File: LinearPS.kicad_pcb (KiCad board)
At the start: 2 copper layers, 100 x 100 mm, 100 parts, among them J1 Conn_01x03, J10 Conn_01x01, J11 Conn_01x01, J12 Conn_01x01, J14 Conn_01x01, J2 Conn_01x02, J3 Conn_01x03, J4 Conn_01x01, J5 Conn_01x01, J6 Conn_01x01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

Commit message: Fixed several layout issues, added a couple of resistors to ensure stability
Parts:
- added R33: 1k, Resistors_THT:R_Axial_DIN0411_L9.9mm_D3.6mm_P12.70mm_Horizontal, F.Cu at (147.5, 141.0)
- added R35: 1M, Resistors_THT:R_Axial_DIN0207_L6.3mm_D2.5mm_P7.62mm_Horizontal, F.Cu at (118.5, 62.0)
- R24, R25, R26, R27, R7: value 0R24 -> 0R47
- moved J2 10.4 mm to (141.9, 118.0)
- moved R17 9.19 mm to (140.8, 67.4)
- moved R40 6.93 mm to (120.7, 64.8), turned to 0 degrees
- moved J9 3.56 mm to (142.4, 60.5)
- moved U3 2.86 mm to (127.6, 75.4)
- moved R29 0.90 mm to (129.8, 81.8)
- moved RV2 0.49 mm to (142.5, 71.8)
- moved C14 0.28 mm to (136.7, 64.8)
- moved R38 0.21 mm to (128.3, 62.0)
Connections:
- Q2 pad 1: Net-(C9-Pad1) -> Net-(Q2-Pad1)
- R29 pad 1: Net-(R29-Pad1) -> GND
- R29 pad 2: GND -> Net-(R29-Pad2)
- R34 pad 1: Net-(JP4-Pad3) -> Net-(JP4-Pad1)
- R34 pad 2: Net-(R29-Pad1) -> Net-(R29-Pad2)
- RV2 pad 2: Net-(JP4-Pad1) -> Net-(JP4-Pad3)
- U3 pad 1: Net-(JP4-Pad3) -> Net-(JP4-Pad1)
- U3 pad 2: Net-(R29-Pad1) -> Net-(R29-Pad2)
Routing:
- net Net-(J9-Pad2): track 22.0 -> 50.0 mm
- net Net-(C9-Pad1): track 105.2 -> 78.3 mm
- net Net-(JP4-Pad1): track 53.3 -> 31.4 mm
- net Net-(JP4-Pad3): track 39.5 -> 60.8 mm
- net Net-(Q2-Pad1): track 0.00 -> 15.0 mm
- net Net-(R29-Pad2): track 0.00 -> 12.5 mm
- net Net-(C4-Pad1): track 172.2 -> 160.2 mm
- net Net-(R29-Pad1): track 12.0 -> 0.00 mm
- net Net-(C15-Pad1): track 19.9 -> 9.43 mm
- net Net-(R17-Pad1): track 15.2 -> 5.61 mm
- net Net-(C6-Pad1): track 162.0 -> 152.5 mm
- net Net-(JP5-Pad3): track 29.3 -> 23.6 mm
- net Net-(Q2-Pad3): track 172.2 -> 166.9 mm
- net Net-(J9-Pad1): track 34.7 -> 39.1 mm
- net Net-(C15-Pad2): track 26.7 -> 23.8 mm
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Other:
- board text added: "CONSTANT CURRENT, CONSTANT VOLTAGE SUPPLY 0-30 VDC, 20 mA-10 A PCB D MARKS CC-BY-SA 4.0"
- board text removed: "CONSTANT CURRENT, CONSTANT VOLTAGE SUPPLY 0-30 VDC, 20 mA-20 A PCB D MARKS CC-BY-SA 4.0"

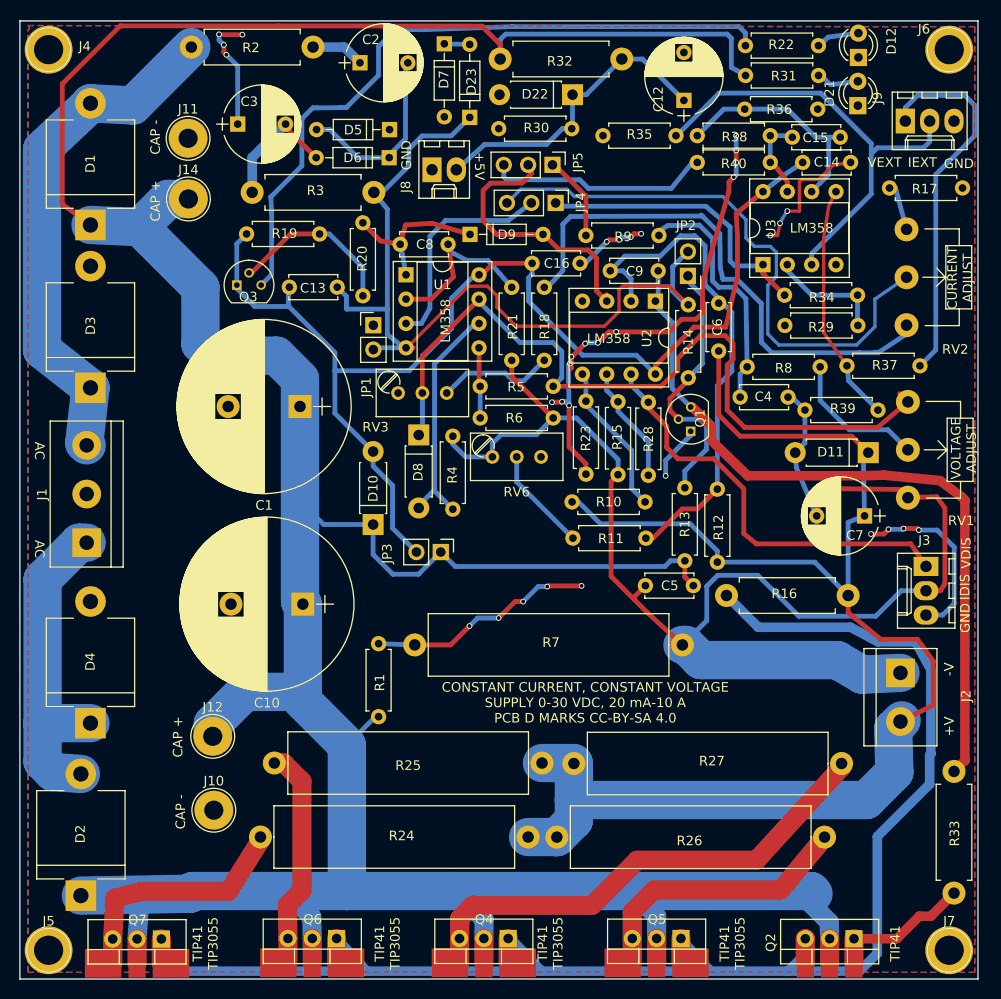
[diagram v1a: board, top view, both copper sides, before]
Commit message: Added extra pin to get reference voltage
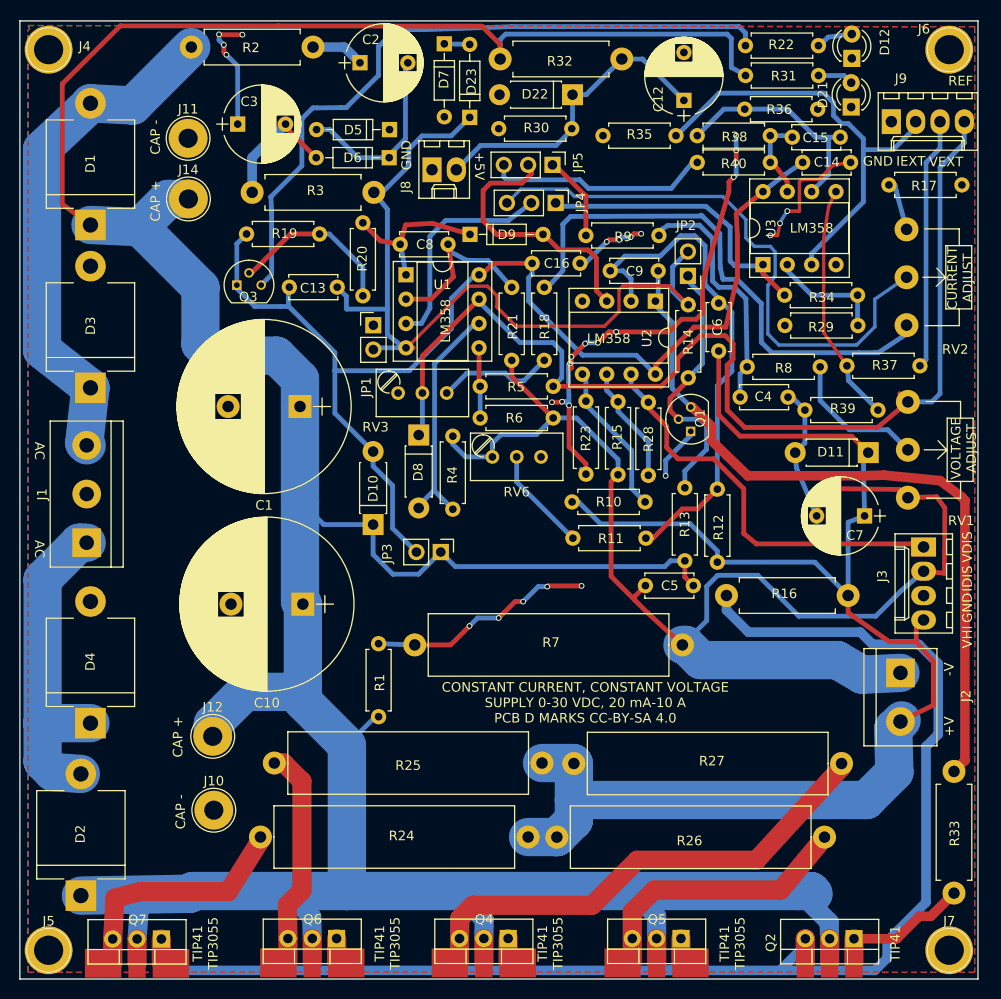
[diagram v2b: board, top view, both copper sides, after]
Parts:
- J3, J9: value Conn_01x03 -> Conn_01x04; footprint Connectors_Molex:Molex_KK-6410-03_03x2.54mm_Straight -> Connectors_Molex:Molex_KK-6410-04_04x2.54mm_Straight
- R37, R39: value 10k -> 100k
- moved J3 2.05 mm to (144.3, 104.9)
- moved J9 1.46 mm to (141.0, 60.5)
- moved D21 0.71 mm to (136.8, 59.0)
- moved D12 0.70 mm to (136.8, 53.9)
- moved R17 0.32 mm to (140.7, 67.1)
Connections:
- J9 pad 1: Net-(J9-Pad1) -> GND
- J9 pad 3: GND -> Net-(J9-Pad3)
- R37 pad 2: Net-(J9-Pad1) -> Net-(J9-Pad3)
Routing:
- net Net-(J9-Pad1): track 39.1 -> 0.00 mm
- net Net-(D8-Pad1): track 84.5 -> 117.7 mm
- net Net-(J9-Pad3): track 0.00 -> 26.3 mm
- net GND: track 140.2 -> 121.2 mm, vias 33 -> 29
- net Net-(C6-Pad1): track 152.5 -> 154.9 mm
- net Net-(J9-Pad2): track 50.0 -> 48.2 mm
- net Net-(J3-Pad1): track 44.4 -> 42.9 mm
- net Net-(C4-Pad1): track 160.2 -> 159.4 mm
- net Net-(D12-Pad2): track 5.93 -> 5.23 mm
- net Net-(D21-Pad2): track 4.53 -> 4.00 mm
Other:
- board text added: "REF"
- board text added: "VHI"
